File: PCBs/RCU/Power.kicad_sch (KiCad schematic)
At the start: 30 parts, among them J100 Conn_01x02, U100 AP63203WU, U102 AZ1117-3.3, U103 AP63203WU

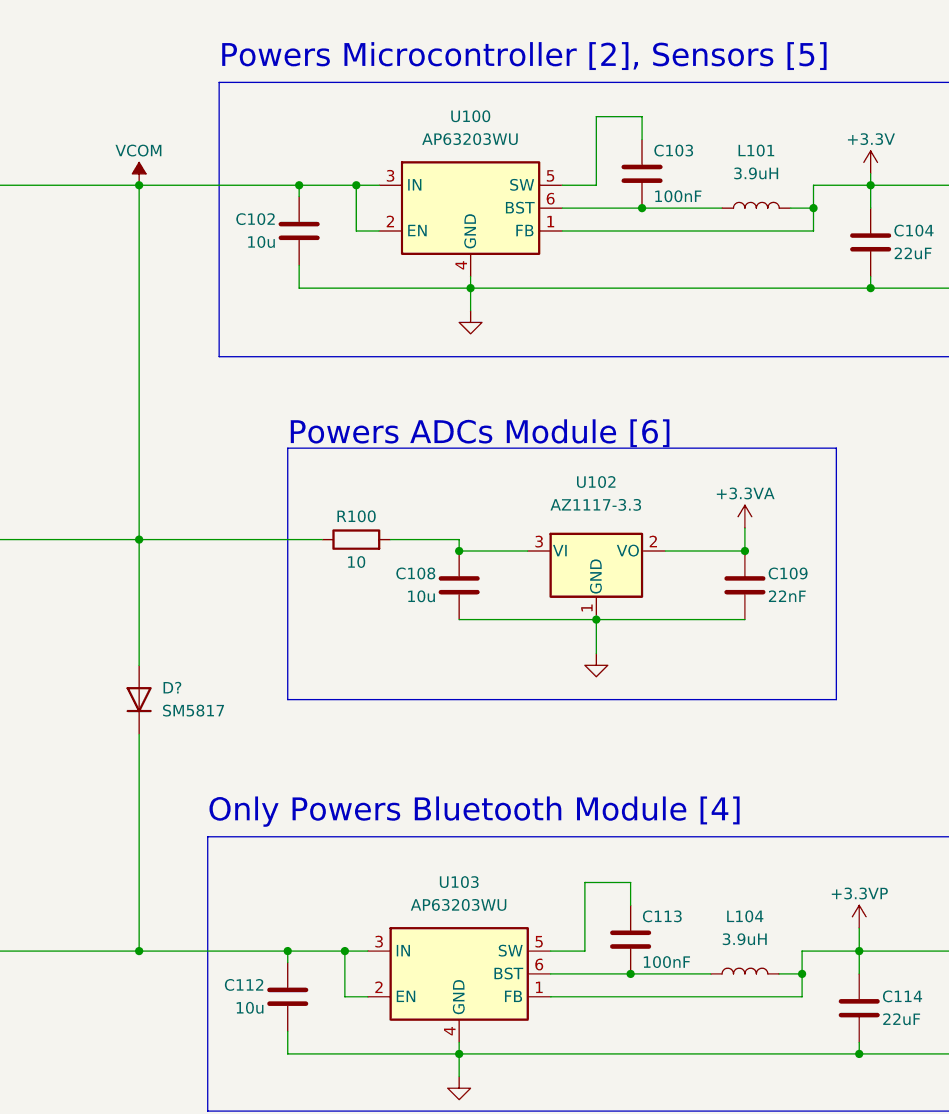
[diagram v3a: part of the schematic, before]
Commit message: Updated switching regulator inductor values and annotated 4th diode in power schematic
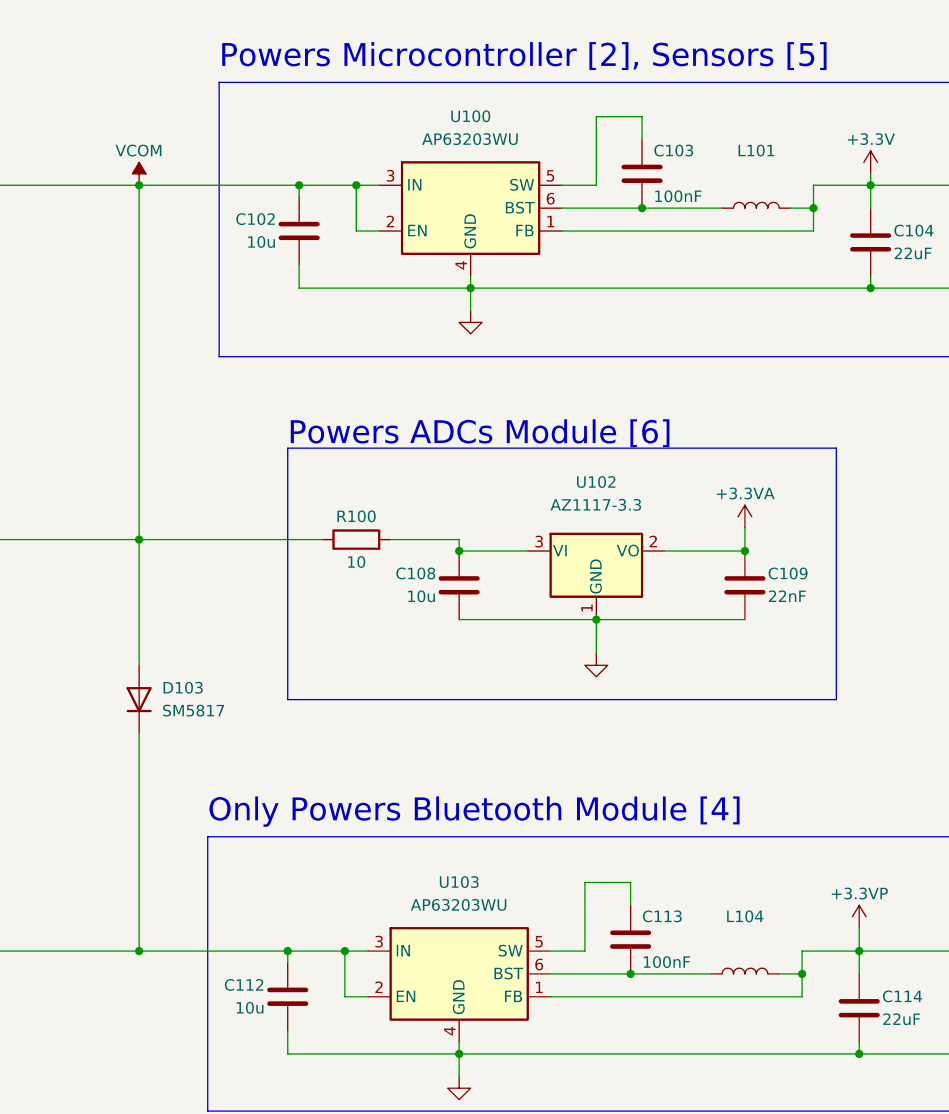
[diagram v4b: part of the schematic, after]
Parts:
- L101, L104: value 3.9uH -> (none)
- gave numbers to parts that had none: 1
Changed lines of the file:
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@@
     (in_bom yes) (on_board yes) (fields_autoplaced)
     (property "Reference" "L101" (id 0) (at 213.36 52.07 90))
-    (property "Value" "3.9uH" (id 1) (at 213.36 54.61 90))
+    (property "Value" "" (id 1) (at 213.36 54.61 90))
     (property "Footprint" "" (id 2) (at 213.36 58.42 0)
       (effects (font (size 1.27 1.27)) hide)
@@
     (in_bom yes) (on_board yes) (fields_autoplaced)
     (property "Reference" "L104" (id 0) (at 212.09 137.16 90))
-    (property "Value" "3.9uH" (id 1) (at 212.09 139.7 90))
+    (property "Value" "" (id 1) (at 212.09 139.7 90))
     (property "Footprint" "" (id 2) (at 212.09 143.51 0)
       (effects (font (size 1.27 1.27)) hide)
@@
   (symbol (lib_id "Diode:SM513") (at 144.78 113.03 90) (unit 1)
     (in_bom yes) (on_board yes) (fields_autoplaced)
-    (property "Reference" "D?" (id 0) (at 147.32 111.7599 90)
+    (property "Reference" "D103" (id 0) (at 147.32 111.7599 90)
       (effects (font (size 1.27 1.27)) (justify right))
     )

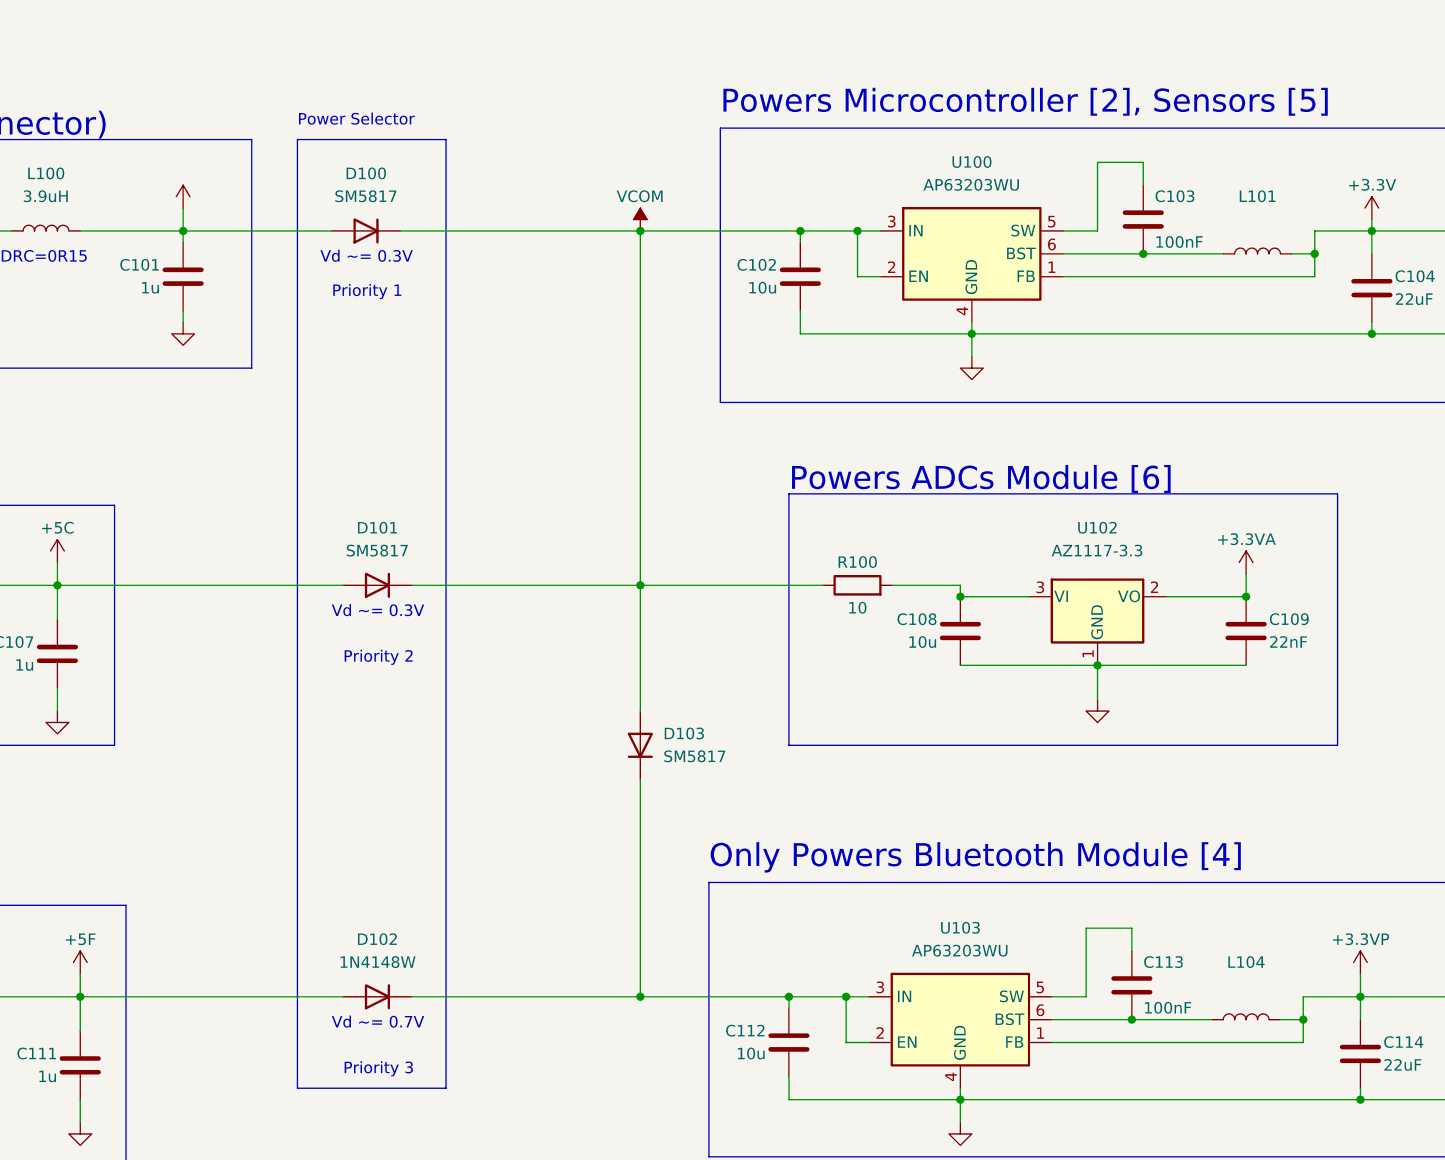
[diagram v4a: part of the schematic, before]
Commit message: Use Rext = 0 ohms for oscillator circuit
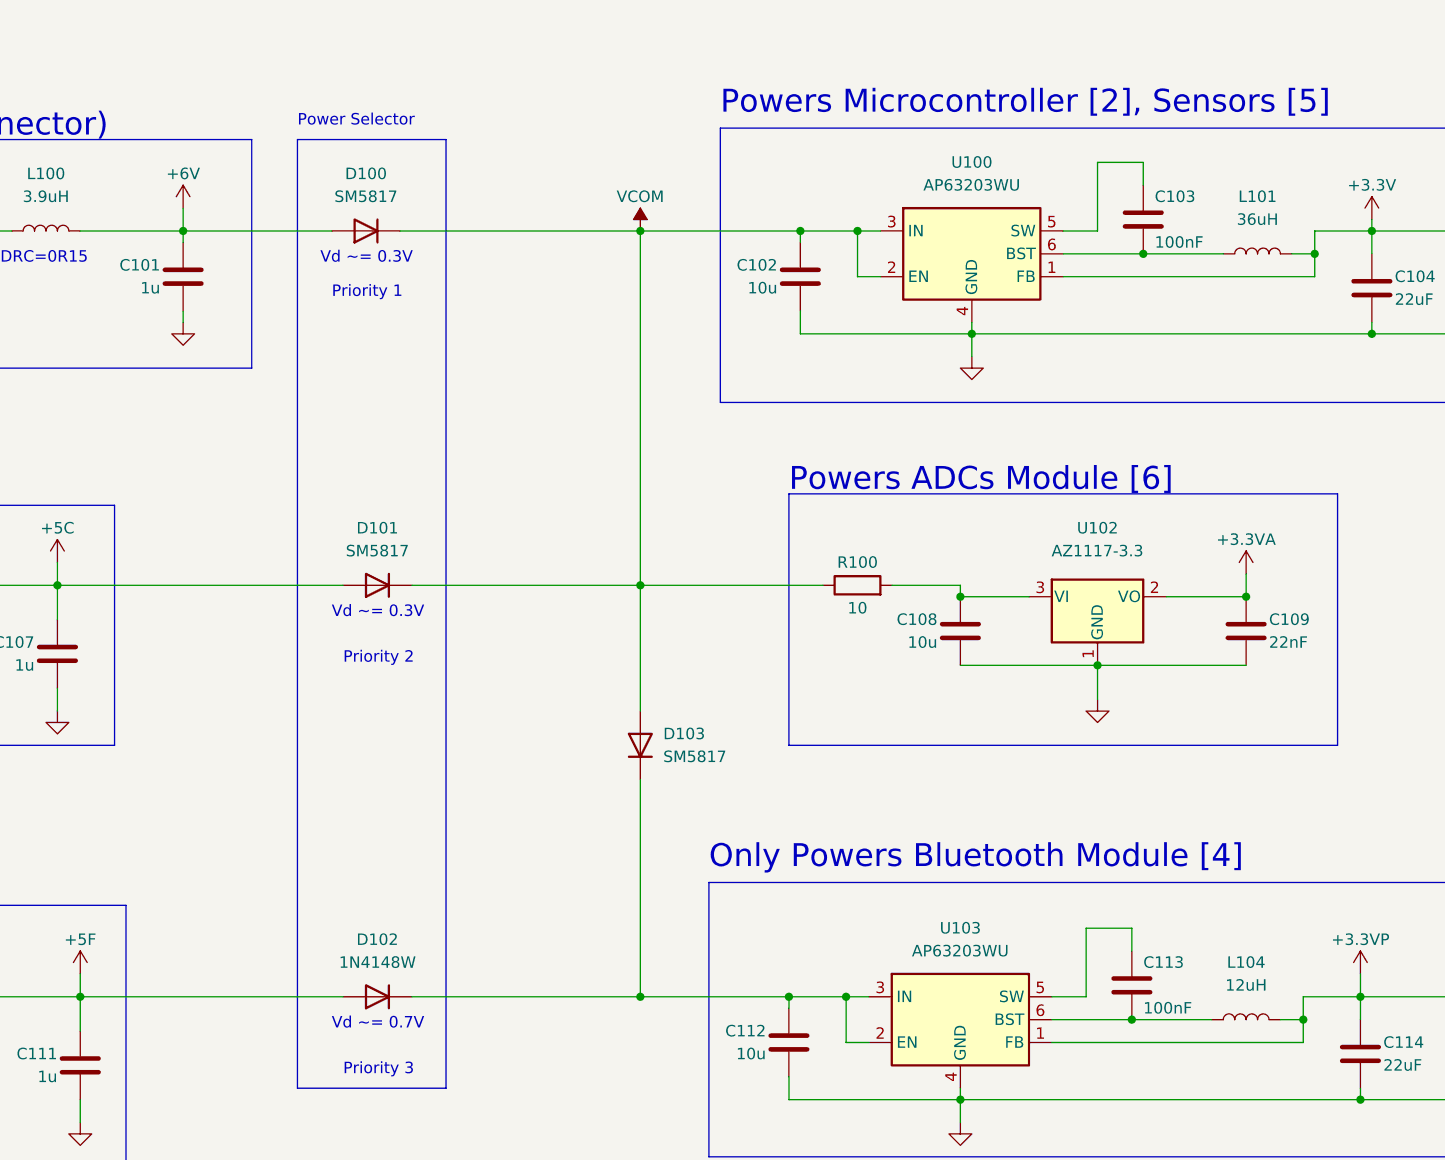
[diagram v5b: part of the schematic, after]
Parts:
- L101: value (none) -> 36uH
- L104: value (none) -> 12uH
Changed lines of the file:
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@@
     (in_bom yes) (on_board yes) (fields_autoplaced)
     (property "Reference" "L101" (id 0) (at 213.36 52.07 90))
-    (property "Value" "" (id 1) (at 213.36 54.61 90))
+    (property "Value" "36uH" (id 1) (at 213.36 54.61 90))
     (property "Footprint" "" (id 2) (at 213.36 58.42 0)
       (effects (font (size 1.27 1.27)) hide)
@@
     (in_bom yes) (on_board yes) (fields_autoplaced)
     (property "Reference" "L104" (id 0) (at 212.09 137.16 90))
-    (property "Value" "" (id 1) (at 212.09 139.7 90))
+    (property "Value" "12uH" (id 1) (at 212.09 139.7 90))
     (property "Footprint" "" (id 2) (at 212.09 143.51 0)
       (effects (font (size 1.27 1.27)) hide)
@@
       (effects (font (size 1.27 1.27)) hide)
     )
-    (property "Value" "" (id 1) (at 93.98 49.53 0))
+    (property "Value" "+6V" (id 1) (at 93.98 49.53 0))
     (property "Footprint" "" (id 2) (at 93.98 53.34 0)
       (effects (font (size 1.27 1.27)) hide)

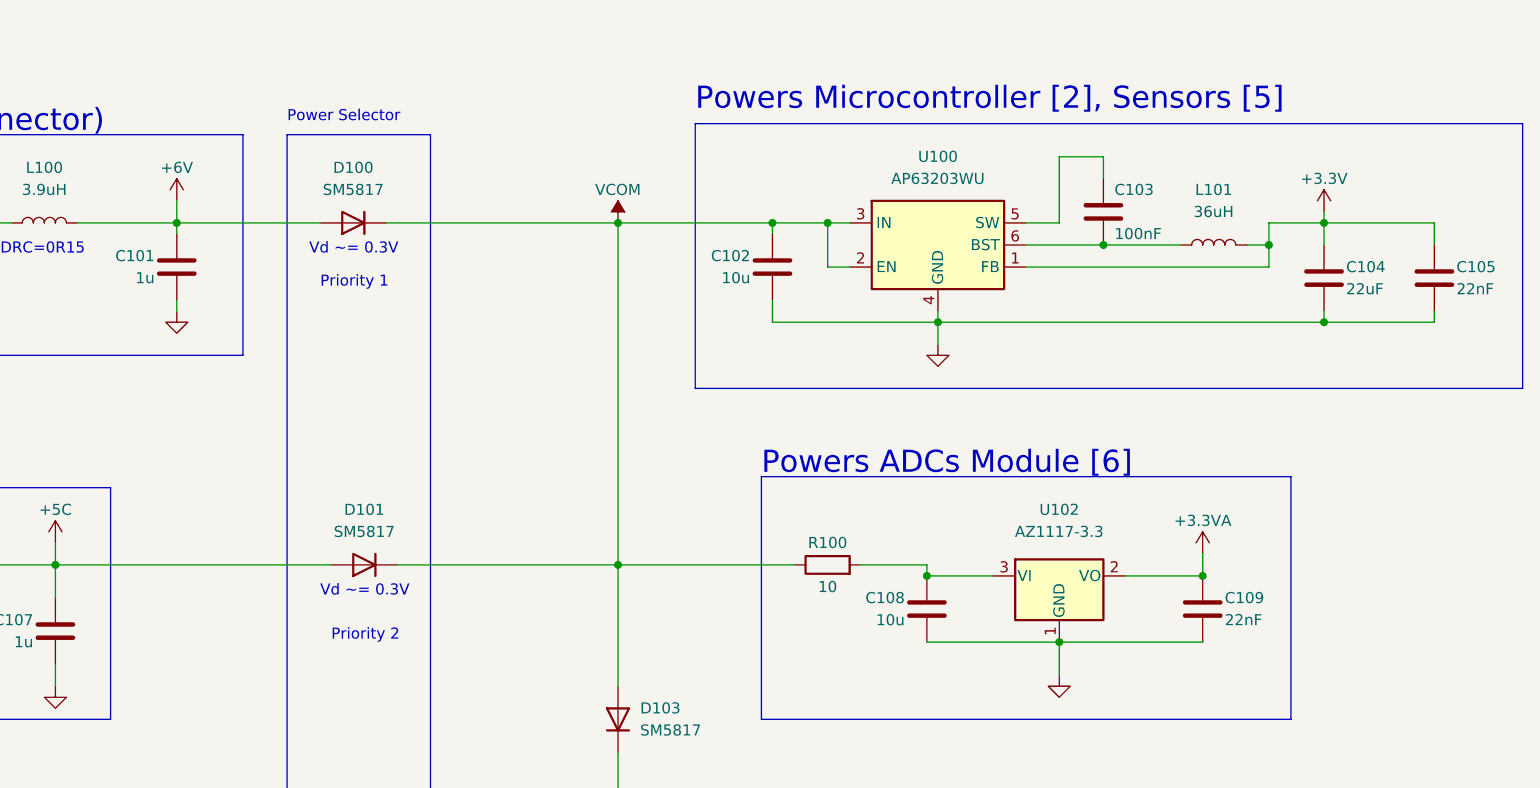
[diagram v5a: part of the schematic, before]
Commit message: Corrected cap values in regulators, changed voltage after battery filter to 9V, will use a 6V regulator to power motors in the near future
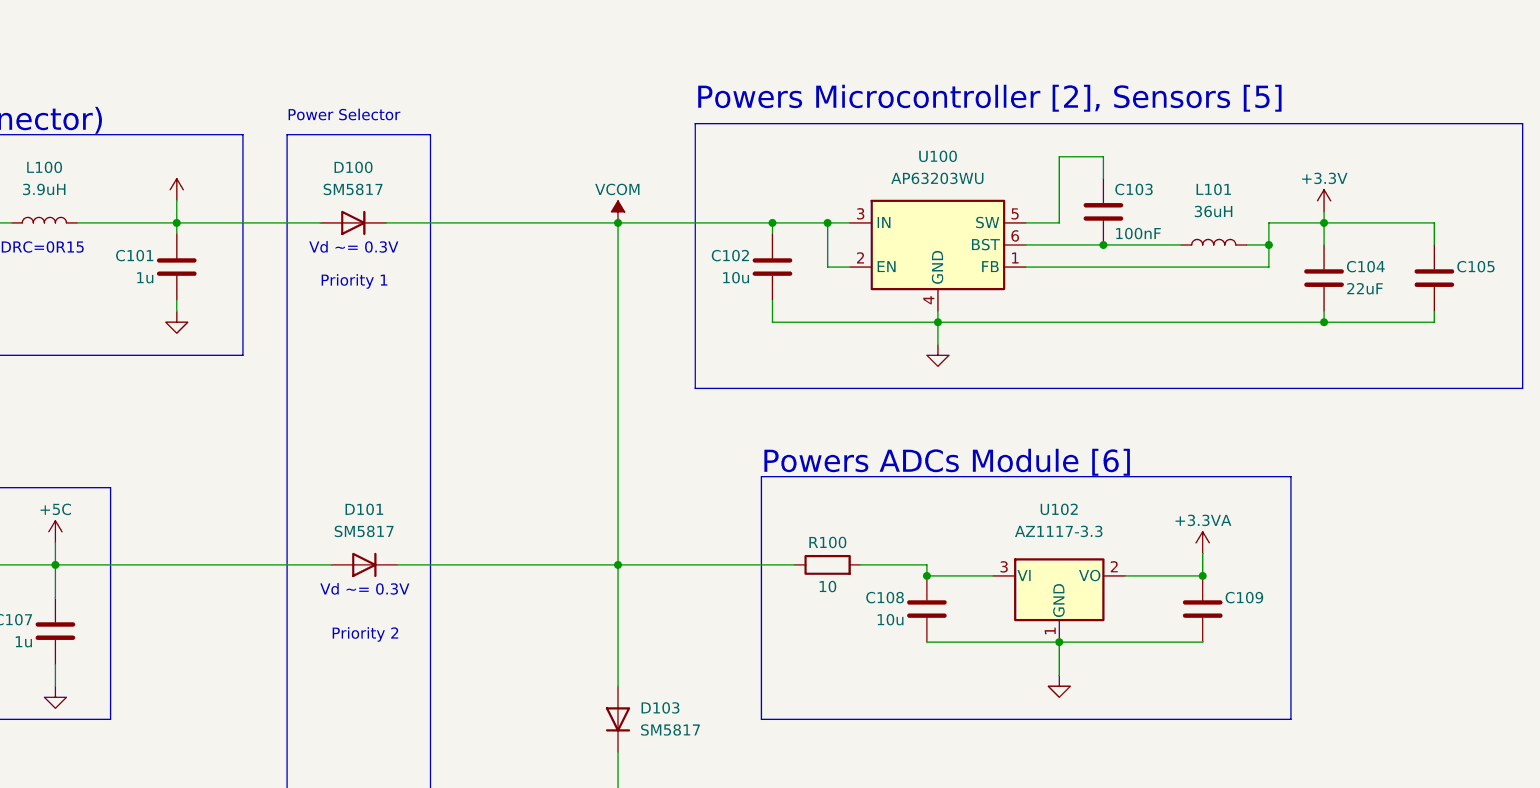
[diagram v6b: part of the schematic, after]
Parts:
- C105, C109: value 22nF -> (none)
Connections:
- net +6V renamed +9V
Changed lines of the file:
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@@
     (pin "2")
+  )
+  (symbol (lib_id "power:+9V") (at 93.98 53.34 0) (unit 1)
+    (in_bom yes) (on_board yes)
+    (property "Reference" "#PWR?" (id 0) (at 93.98 57.15 0)
+      (effects (font (size 1.27 1.27)) hide)
+    )
+    (property "Value" "" (id 1) (at 93.98 49.53 0))
+    (property "Footprint" "" (id 2) (at 93.98 53.34 0)
+      (effects (font (size 1.27 1.27)) hide)
+    )
+    (property "Datasheet" "" (id 3) (at 93.98 53.34 0)
+      (effects (font (size 1.27 1.27)) hide)
+    )
+    (pin "1")
   )
   (symbol (lib_id "Device:C") (at 212.09 100.33 0) (unit 1)
@@
       (effects (font (size 1.27 1.27)) (justify left))
     )
-    (property "Value" "22nF" (id 1) (at 214.63 101.6 0)
+    (property "Value" "" (id 1) (at 214.63 101.6 0)
       (effects (font (size 1.27 1.27)) (justify left))
     )
@@
       (effects (font (size 1.27 1.27)) (justify left))
     )
-    (property "Value" "22nF" (id 1) (at 241.3 63.5 0)
+    (property "Value" "" (id 1) (at 241.3 63.5 0)
       (effects (font (size 1.27 1.27)) (justify left))
     )
@@
     (pin "2")
   )
-  (symbol (lib_id "power:+6V") (at 93.98 53.34 0) (unit 1)
-    (in_bom yes) (on_board yes)
-    (property "Reference" "#PWR?" (id 0) (at 93.98 57.15 0)
-      (effects (font (size 1.27 1.27)) hide)
-    )
-    (property "Value" "+6V" (id 1) (at 93.98 49.53 0))
-    (property "Footprint" "" (id 2) (at 93.98 53.34 0)
-      (effects (font (size 1.27 1.27)) hide)
-    )
-    (property "Datasheet" "" (id 3) (at 93.98 53.34 0)
-      (effects (font (size 1.27 1.27)) hide)
-    )
-    (pin "1")
-  )
   (symbol (lib_id "Device:C") (at 64.77 60.96 0) (mirror y) (unit 1)
